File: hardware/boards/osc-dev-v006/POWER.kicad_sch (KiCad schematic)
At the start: 16 parts, among them J1 JST-PH-H, J2 TERM, U1 HT7533-1

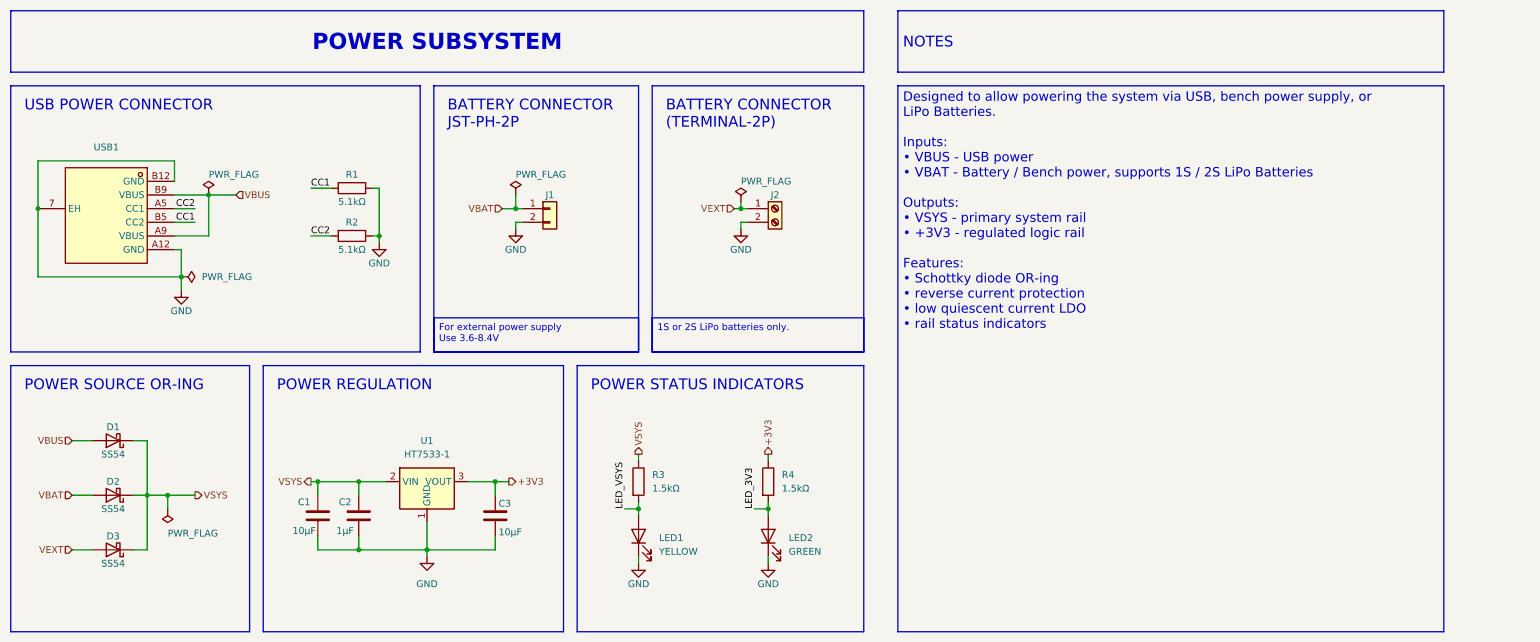
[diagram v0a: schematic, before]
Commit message: OSC DEV CH32 REV B (#10)
* update board

* updated schematics. ERC on schematics is now passing

* completed routing.

* adding ground vias

* update schematics notes

* update bom and component properties

* use red header pins for jumpers

* rename board to osc-dev-v006

* add docs
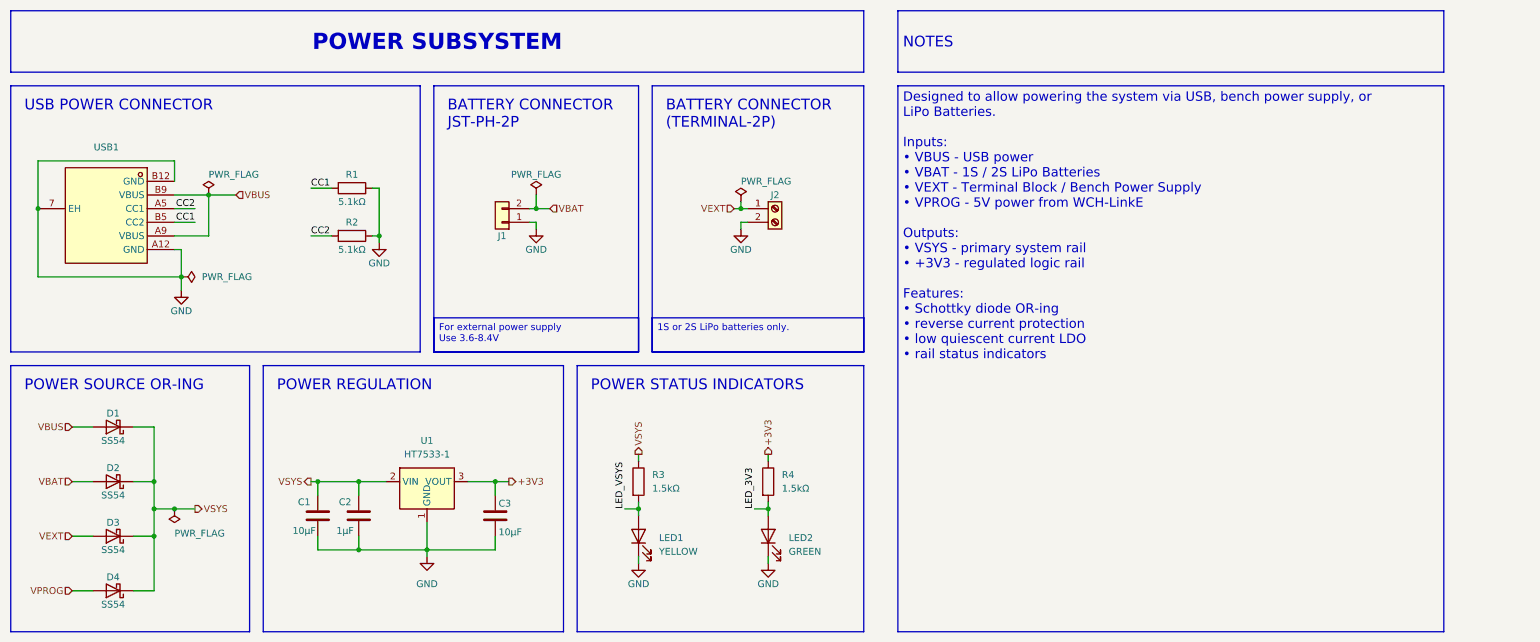
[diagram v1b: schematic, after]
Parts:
- added D4: SS54, Diode_SMD:D_SMA_Handsoldering, symbol Diode:SS34
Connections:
- net GND: now also J1.1 (Pin_1); no longer J1.2 (Pin_2)
- net VBAT: now also J1.2 (Pin_2); no longer J1.1 (Pin_1)
- net VSYS: now also D4.1 (K)
- new net VPROG: D4.2 (A)
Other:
- moved on the sheet: D1, D2, D3, J1
